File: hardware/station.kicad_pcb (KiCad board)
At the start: 2 copper layers, 100 x 60 mm, 168 parts, among them J1 AudioJack3, J2 AudioJack3, J3 Conn_02x05_Odd_Even, J4 Conn_02x05_Counter_Clockwise, J5 Screw_Terminal_01x02, Q1 NTMFS5C682NL, Q2 NTMFS5C682NL, Q3 FDV301N, Q4 FDV301N, Q5 DMP2120U, Q6 DMP2120U, Q7 NTMFS5C682NL, Q8 NTMFS5C682NL, U1 NCS213, U10 LM5109BSD, U11 STM32G431CBT6, U2 MAX44246, U3 LM5109BSD, U4 NCP700BSN30T1G, U5 MCP1501T-25E, U6 LM5164DDAR, U7 LM63615-Q1PWP, U8 NCS213, U9 MAX44246

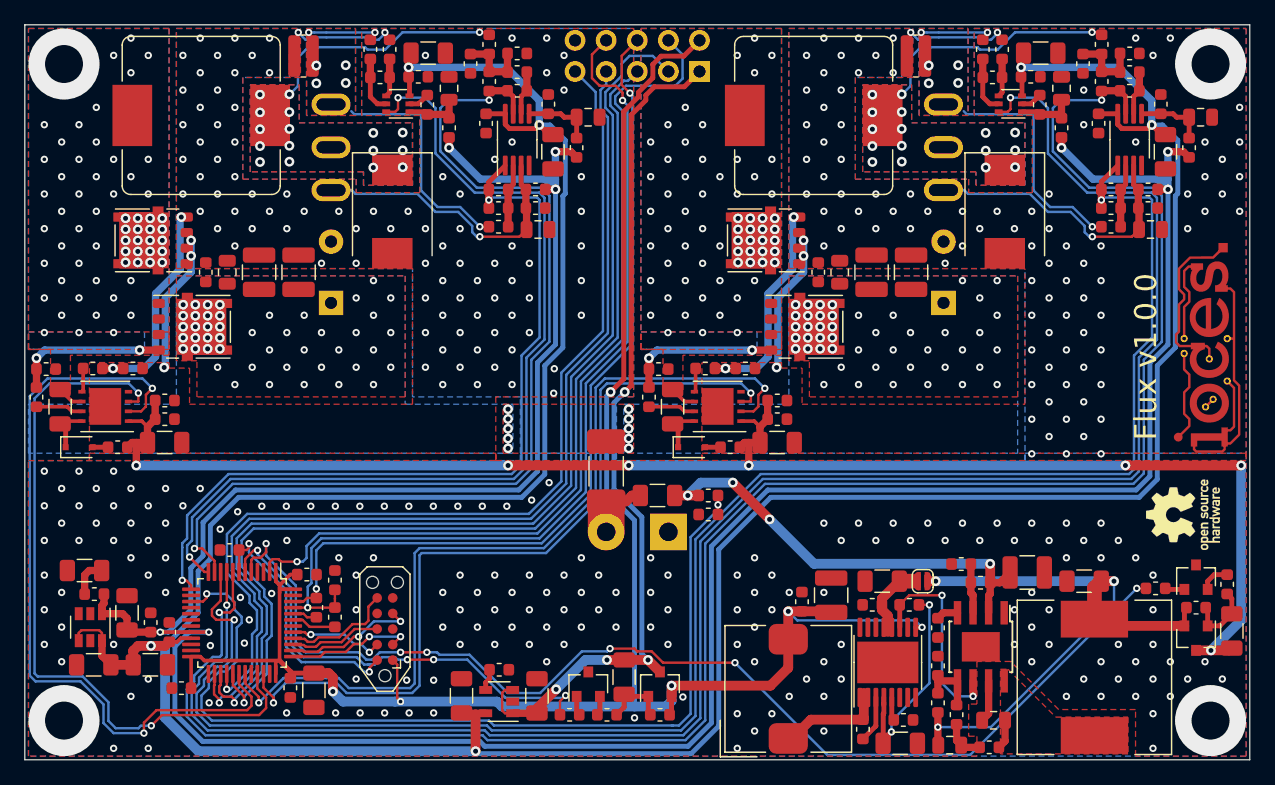
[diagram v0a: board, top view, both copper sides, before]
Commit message: Newly converted schematics, project and symbol libraries
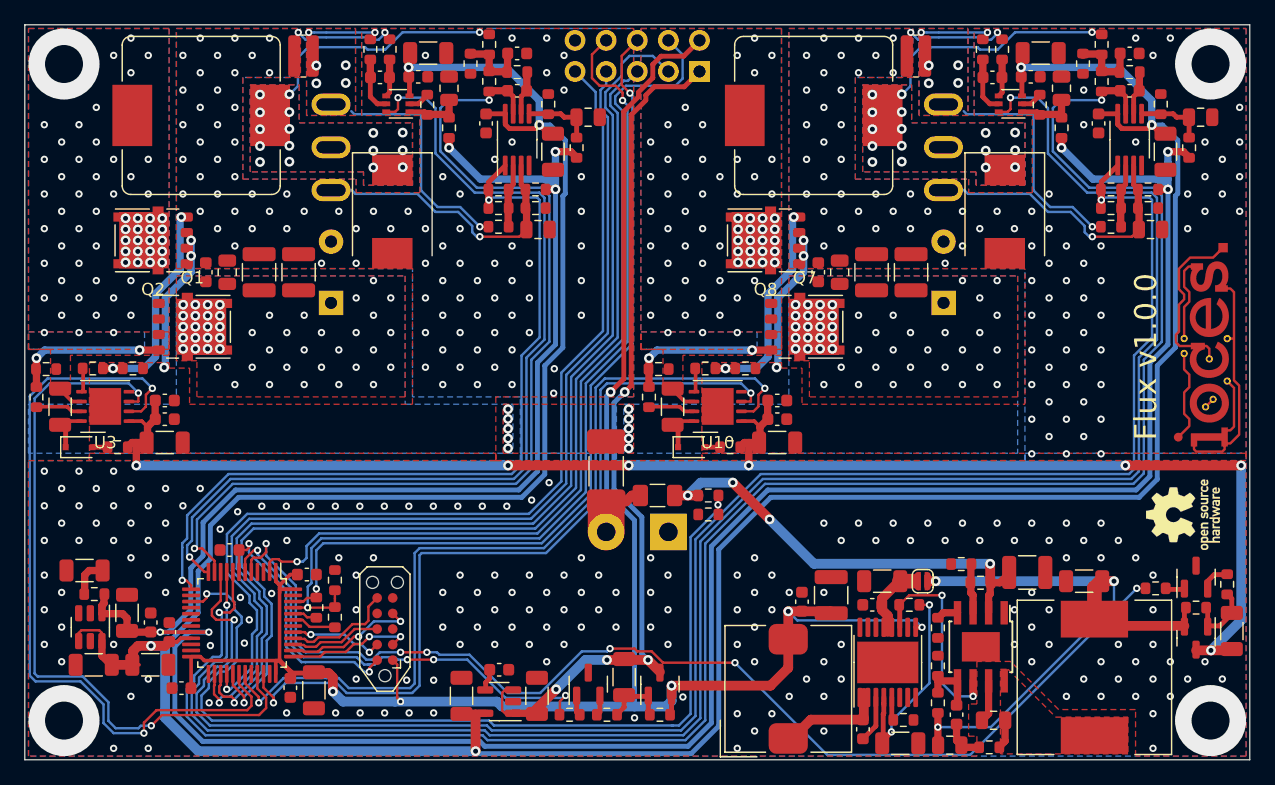
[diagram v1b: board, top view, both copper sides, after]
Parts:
- U10, U3: footprint Package_SON:WSON-8_4x4mm_P0.8mm -> Package_SON:WSON-8-1EP_4x4mm_P0.8mm_EP2.6x3mm
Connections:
- net /Microcontroller/CHA_CUR renamed /Channel A/CUR
- net /Microcontroller/CHA_HI renamed /Channel A/HI
- net /Microcontroller/CHA_LO renamed /Channel A/LO
- net /Microcontroller/CHA_TEMP renamed /Channel A/TEMP
- net /Microcontroller/CHA_VOL renamed /Channel A/VOL
- net /Microcontroller/CHB_CUR renamed /Channel B/CUR
- net /Microcontroller/CHB_HI renamed /Channel B/HI
- net /Microcontroller/CHB_LO renamed /Channel B/LO
- net /Microcontroller/CHB_TEMP renamed /Channel B/TEMP
- net /Microcontroller/CHB_VOL renamed /Channel B/VOL
- net /Microcontroller/~RST renamed /Microcontroller/~{RST}
- net /Microcontroller/~TRST renamed /Microcontroller/~{TRST}
- J4 pad 7: Net-(J4-Pad7) -> unconnected-(J4-Pad7)
- U11 pad 14: Net-(U11-Pad14) -> unconnected-(U11-Pad14)
- U11 pad 16: Net-(U11-Pad16) -> unconnected-(U11-Pad16)
- U11 pad 17: Net-(U11-Pad17) -> unconnected-(U11-Pad17)
- U11 pad 18: Net-(U11-Pad18) -> unconnected-(U11-Pad18)
- U11 pad 22: Net-(U11-Pad22) -> unconnected-(U11-Pad22)
- U11 pad 25: Net-(U11-Pad25) -> unconnected-(U11-Pad25)
- U11 pad 3: Net-(U11-Pad3) -> unconnected-(U11-Pad3)
- U11 pad 32: Net-(U11-Pad32) -> unconnected-(U11-Pad32)
- U11 pad 4: Net-(U11-Pad4) -> unconnected-(U11-Pad4)
- U11 pad 42: Net-(U11-Pad42) -> unconnected-(U11-Pad42)
- U7 pad 14: Net-(U7-Pad14) -> unconnected-(U7-Pad14)
- U7 pad 8: Net-(U7-Pad8) -> unconnected-(U7-Pad8)
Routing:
- net /Microcontroller/EN_12V: track 94.6 -> 0.00 mm, vias 6 -> 0
- net +3V3: track 71.5 -> 166.1 mm, vias 4 -> 10
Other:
- net class Default removed
- net class HV removed
